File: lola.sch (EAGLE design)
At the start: 1 part, among them U1 ATMEGA328P_TQFP

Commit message: Base modules
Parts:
- added C1, C11, C14, C2, C3, C4, C7, C8, C9: 0.1uF, resistor:C-EUC0603
- added C10, C12, C13: 4.7uF, resistor:C-EUC0603
- added C5, C6: 22pF, resistor:C-EUC0603
- added CN1: (no value), adafruit:USBMINIB
- added D1, D2: transil, SparkFun-DiscreteSemi:DIODE-SCHOTTKY-BAT20J
- added D3: DIODE-SCHOTTKY-B340A, SparkFun-DiscreteSemi:DIODE-SCHOTTKY-B340A
- added F1, F3: 6V/0.5A, SparkFun-Fuses:PPTC_HALF-AMP
- added F2: (no value), adafruit:PTCFUSE-1812
- added IC1: FT232RL, ftdichip:FT232RL
- added IC2: MCP73833-UN, adafruit:MCP73833-UN
- added L1: LQH32PN4R7NN0L, rcl:L-EUL1812
- added LED1, LED2: (no value), adafruit:LEDCHIPLED_0805
- added Q1: MOSFET_PCH-DMG2307L, SparkFun-DiscreteSemi:MOSFET_PCH-DMG2307L
- added R1, R5, R6, R9: 10K, resistor:R-EU_R0603
- added R2: 1M, resistor:R-EU_R0603
- added R3, R4: 1K, resistor:R-EU_R0603
- added R7: 2K, resistor:R-EU_R0603
- added R8: 10K ntc, resistor:R-EU_R0603
- added U$1: MCP1603T-330I/OS, MCP1603T-330I_OS:MCP1603T-330I/OS
- added U$2, U$3: COMF_BHC-18650-1P, FloManEagle:COMF_BHC-18650-1P
- added U2: RFM69HW, SparkFun-RF:RFM69HW
- added U3: AT24C256C-SSHL-T, AT24C256C-SSHL-T:AT24C256C-SSHL-T
- added U4: ADS1115IDGST, ADS1115IDGST:ADS1115IDGST
- added X1: (no value), adafruit:SMACONNECTOR_EDGE_UFL
- added Y1: 8MHz, SparkFun-Clocks:CRYSTAL-GROUNDEDSMD-5X3.2
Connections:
- new net !EXT_RESET: C8.2, IC1.!RTS
- new net !RESET: C8.1, R1.2, U1.PC6(/RESET)
- new net 3.3V: C1.1, C10.1, C11.1, C14.1, C2.1, C3.1, C4.1, C9.1, F3.2, R1.1, R5.2, R6.2, U1.AREF, U1.AVCC, U1.VCC@4, U1.VCC@6, U2.3.3V, U3.VCC, U4.VDD
- new net 5V: D3.A, F1.2, IC1.VCC, IC2.VDD1, IC2.VDD2, Q1.G, R9.2
- new net ADC_RDY: U4.ALERT/RDY
- new net AIN0: U4.AIN0
- new net AIN1: U4.AIN1
- new net AIN2: U4.AIN2
- new net AIN3: U4.AIN3
- new net CHG: IC2.STAT1
- new net FT_3.3V: C7.1, IC1.3V3OUT, IC1.VCCIO, R3.2, R4.2
- new net FULL: IC2.STAT2
- new net GND: C1.2, C10.2, C11.2, C12.2, C13.2, C14.2, C2.2, C3.2, C4.2, C5.2, C6.2, C7.2, C9.2, CN1.GND, D1.A, D2.A, IC1.GND@A, IC2.GND, R7.2, R8.2, R9.1, U$1.GND, U$2.GND, U$3.GND, U1.AGND, U1.GND@3, U1.GND@5, U2.GND@1, U2.GND@2, U3.A0, U3.A1, U3.A2, U3.GND, U3.WP, U4.ADDR, U4.GND, X1.GND1, X1.GND2, X1.GND3, X1.GND4, Y1.3
- new net MISO: U1.PB4(MISO), U2.MISO
- new net MOSI: U1.PB3(MOSI/OC2), U2.MOSI
- new net N$1: U2.ANT, X1.ANT
- new net N$10: U1.PD4(XCK/T0)
- new net N$11: U1.PD5(T1)
- new net N$12: U1.PD6(AIN0)
- new net N$13: U1.PD7(AIN1)
- new net N$14: U1.PB0(ICP)
- new net N$15: U1.PB1(OC1A)
- new net N$16: U1.PB2(SS/OC1B)
- new net N$17: C5.1, R2.2, U1.PB6(XTAL1/TOSC1), Y1.1
- new net N$18: C6.1, R2.1, U1.PB7(XTAL2/TOSC2), Y1.2
- new net N$19: IC2.THERM, R8.1
- new net N$2: F2.1, U$2.BAT
- new net N$20: CN1.VBUS, F1.1
- new net N$21: CN1.D+, D2.C, IC1.USBDP
- new net N$22: CN1.D-, D1.C, IC1.USBDM
- new net N$23: LED2.A, R4.1
- new net N$24: IC1.CBUS1, LED2.C
- new net N$25: IC1.CBUS0, LED1.C
- new net N$26: LED1.A, R3.1
- new net N$28: IC2.PROG, R7.1
- new net N$29: L1.2, U$1.LX
- new net N$3: C13.1, F3.1, L1.1, U$1.VFB/VOUT
- new net N$4: U1.PC0(ADC0)
- new net N$5: U1.PC1(ADC1)
- new net N$6: U1.PC2(ADC2)
- new net N$7: U1.PC3(ADC3)
- new net N$8: U1.PD2(INT0)
- new net N$9: U1.PD3(INT1)
- new net RF_INT: U2.DIO0
- new net RF_SS: U2.NSS
- new net RX: IC1.TXD, U1.PD0(RXD)
- new net SCK: U1.PB5(SCK), U2.SCK
- new net SCL: R5.1, U1.PC5(ADC5/SCL), U3.SCL, U4.SCL
- new net SDA: R6.1, U1.PC4(ADC4/SDA), U3.SDA, U4.SDA
- new net TX: IC1.RXD, U1.PD1(TXD)
- new net VCC: D3.C, Q1.S, U$1.VIN, U$1.~SHDN
- new net V_BATT: C12.1, F2.2, IC2.VBAT1, IC2.VBAT2, Q1.D, U$3.BAT
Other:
- note added: "A0"
- note added: "A1"
- note added: "A2"
- note added: "A3"

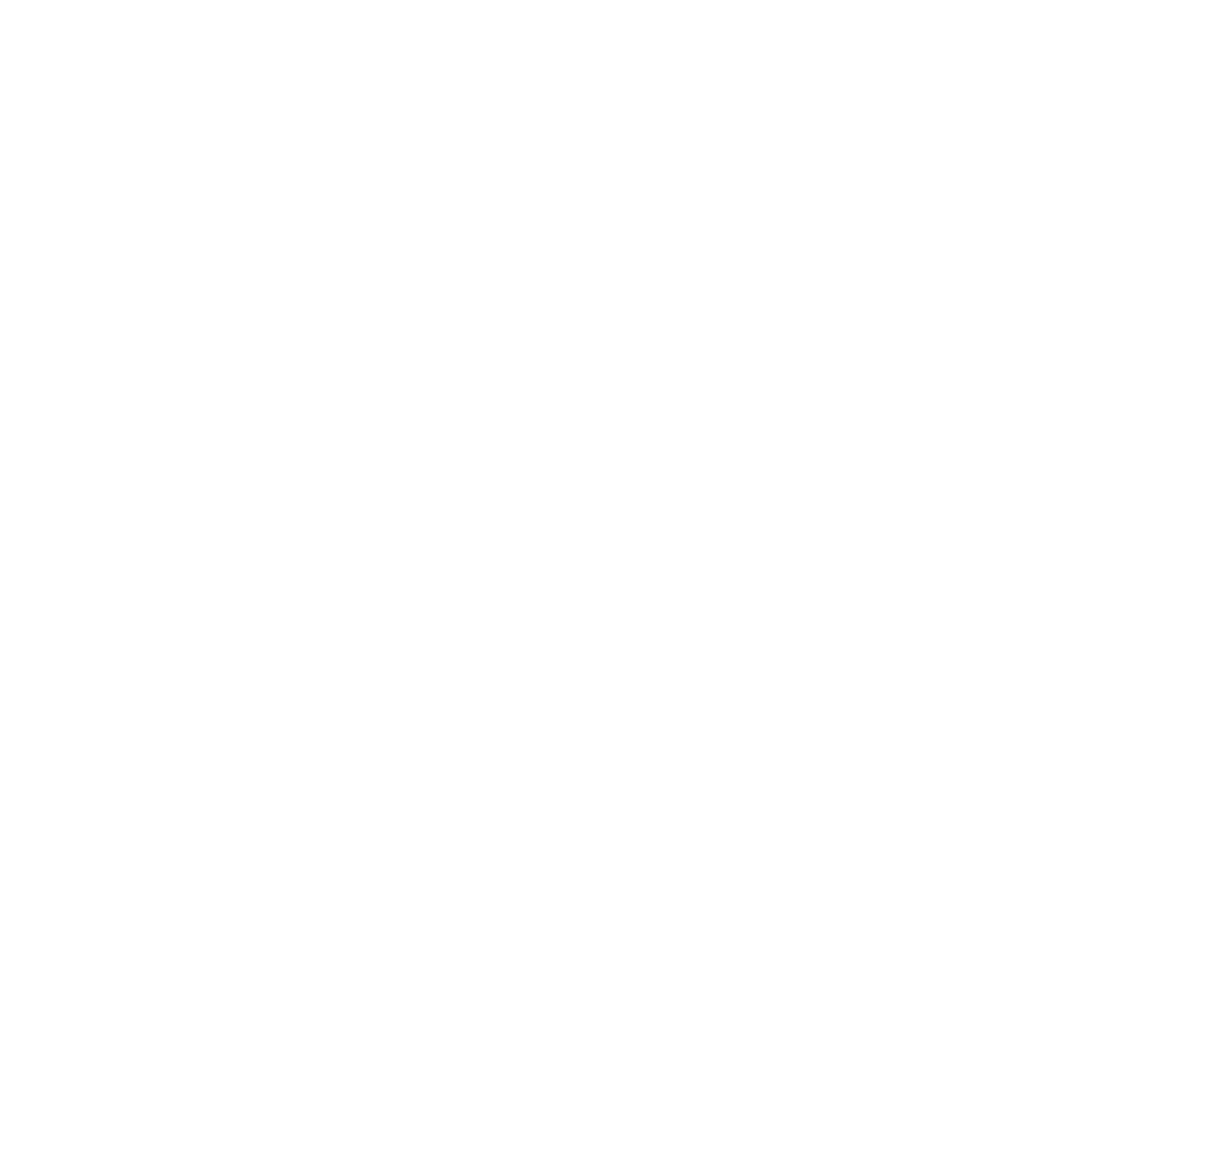
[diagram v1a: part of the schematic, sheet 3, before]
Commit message: StepUp converter plus output-en
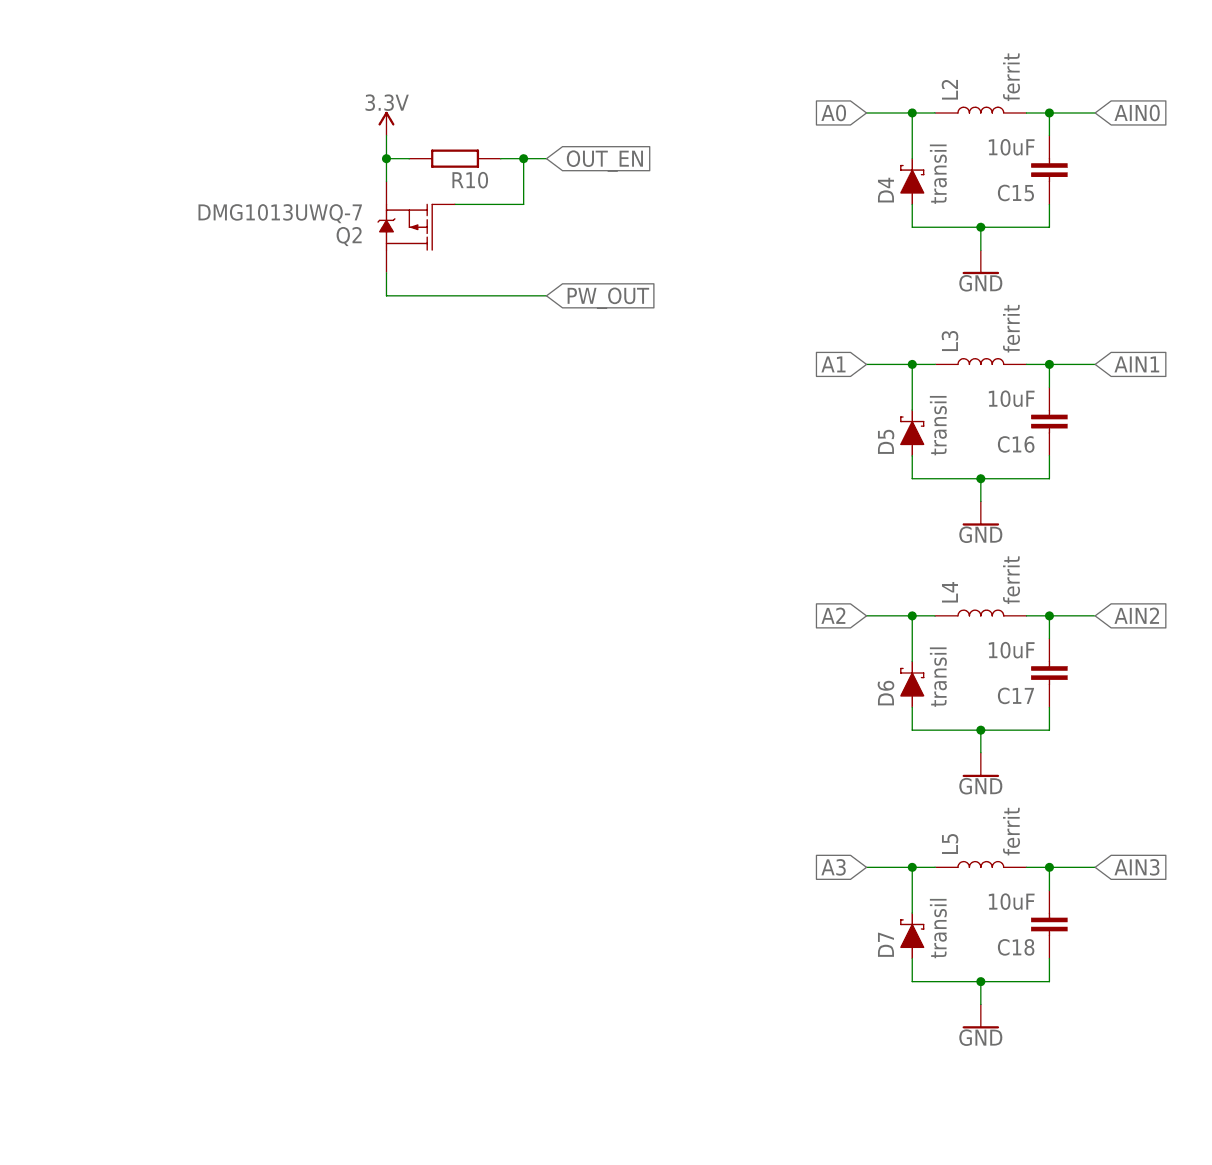
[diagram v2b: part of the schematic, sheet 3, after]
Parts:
- added C15, C16, C17, C18: 10uF, resistor:C-EUC0603
- added C19, C20, C21: 10uF, resistor:C-EUC1206
- added C22: 1uF, resistor:C-EUC0805
- added D4, D5, D6, D7: transil, SparkFun-DiscreteSemi:DIODE-SCHOTTKY-BAT20J
- added L2, L3, L4, L5: ferrit, SparkFun-Coils:INDUCTOR-0603-33NH
- added Q2, Q3: DMG1013UWQ-7, SparkFun-DiscreteSemi:MOSFET_PCH-DMG2307L
- added R10: (no value), resistor:R-EU_R0603
- added R11, R12: 100K, resistor:R-EU_R0603
- added S1: MOMENTARY-SWITCH-SPST-SMD-4.6X2.8MM, SparkFun-Switches:MOMENTARY-SWITCH-SPST-SMD-4.6X2.8MM
- added U$5: MCP1252-33X50I/MS, MCP1252-33X50I_MS:MCP1252-33X50I/MS
- C13: device resistor:C-EUC0603 -> resistor:C-EUC1206
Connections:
- new net 5V_OUT: Q3.D
- new net A0: D4.C, L2.1
- new net A1: D5.C, L3.1
- new net A2: D6.C, L4.1
- new net A3: D7.C, L5.1
- new net BATT_SENSE: R11.1, R12.2
- new net BUCK_EN: U$5.!SHDN
- new net BUCK_PGD: U$5.PGOOD
- new net N$30: C20.1, Q3.S, U$5.VOUT
- new net N$31: C22.1, U$5.C+
- new net N$32: C22.2, U$5.C-
- new net OUT_EN: Q2.G, Q3.G, R10.1
- new net PW_OUT: Q2.D
- net !RESET: now also S1.1
- net 3.3V: now also Q2.S, R10.2
- net AIN0: now also C15.2, L2.2
- net AIN1: now also C16.2, L3.2
- net AIN2: now also C17.2, L4.2
- net AIN3: now also C18.2, L5.2
- net GND: now also C15.1, C16.1, C17.1, C18.1, C19.2, C20.2, C21.1, D4.A, D5.A, D6.A, D7.A, R12.1, S1.2, U$5.GND, U$5.SELECT
- net VCC: now also C21.2
- net V_BATT: now also C19.1, R11.2, U$5.VIN
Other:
- note added: "3.3V DC-DC Converter"
- note added: "5V Buck Converter"
- note added: "Li-ion Charger"
- note added: "X7R Dielectric"
- moved on the sheet: L1

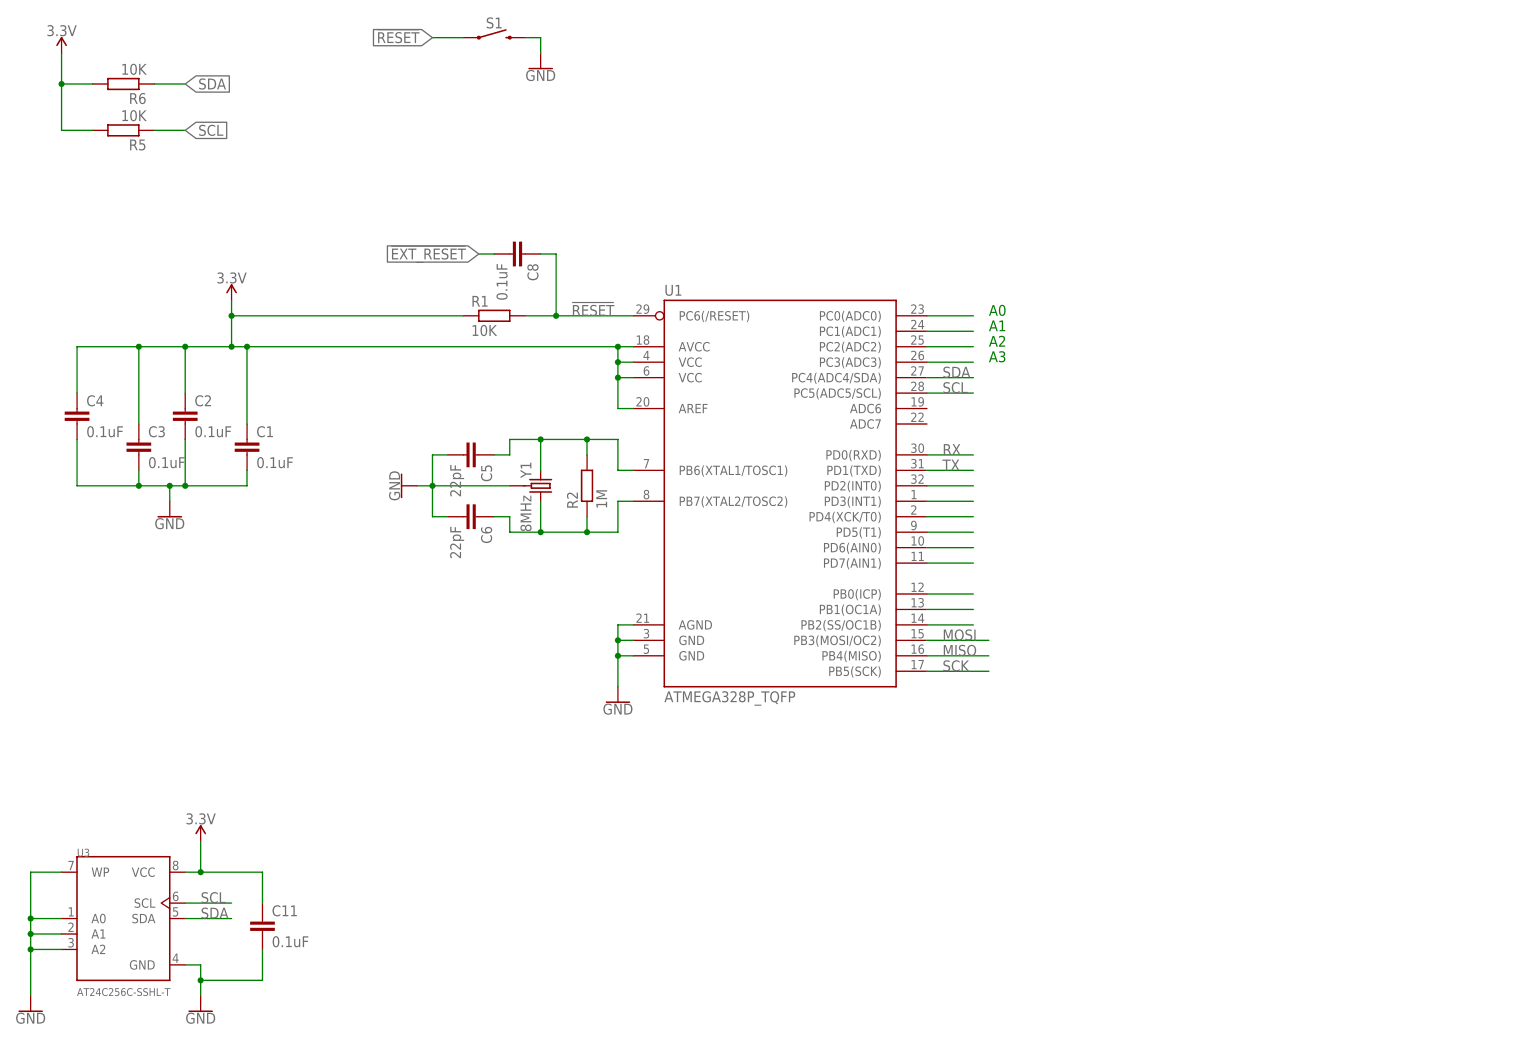
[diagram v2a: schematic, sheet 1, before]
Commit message: rtc, step-up converter
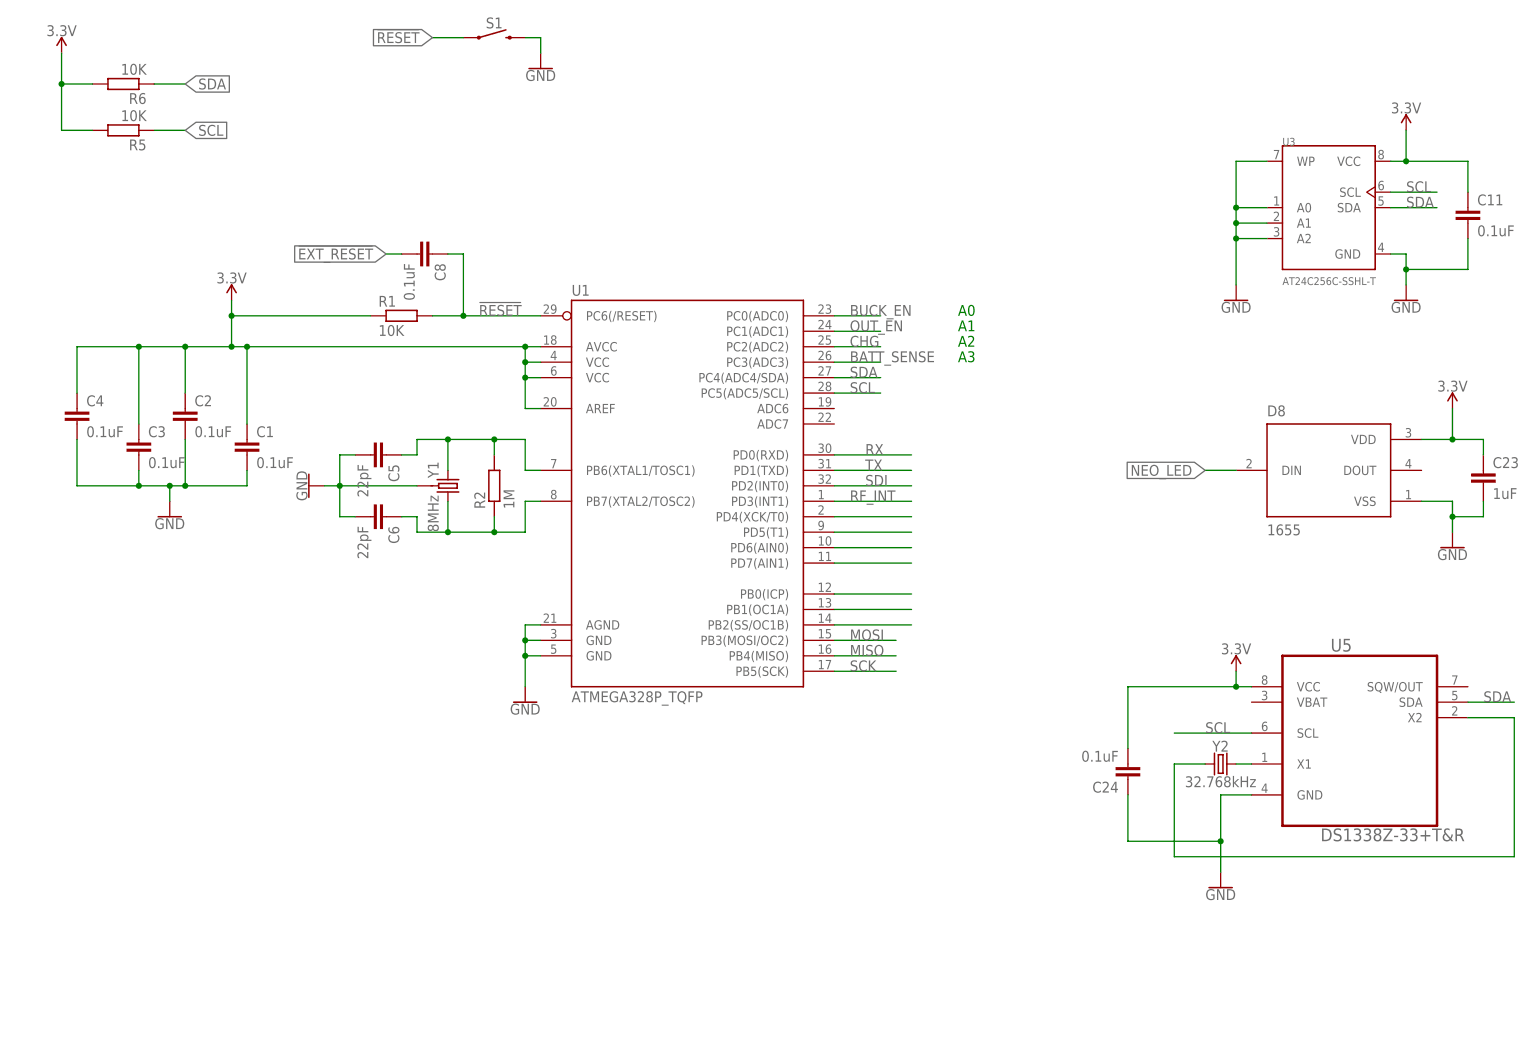
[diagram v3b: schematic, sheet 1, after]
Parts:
- added C23: 1uF, resistor:C-EUC0603
- added C24: 0.1uF, resistor:C-EUC0603
- added D8: 1655, 1655:1655
- added D9: transil, SparkFun-DiscreteSemi:DIODE-SCHOTTKY-BAT20J
- added J4: (no value), SparkFun-Connectors:CONN_025MM
- added J7: (no value), SparkFun-Connectors:CONN_063.5MM-6
- added JP1, JP2, JP3: JUMPER-SMT_2_NO_NO-SILK, SparkFun-Jumpers:JUMPER-SMT_2_NO_NO-SILK
- added LED3, LED4: (no value), adafruit:LEDCHIPLED_0805
- added R13, R14: 2K, resistor:R-EU_R0603
- added U5: DS1338Z-33+T&R, DS1338Z-33_T_R:DS1338Z-33+T&R
- added Y2: 32.768kHz, SparkFun-Clocks:CRYSTAL-32.768KHZSMD-3.2X1.5
- R10: value (none) -> 10K
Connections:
- removed net N$4: U1.PC0(ADC0)
- removed net N$9: U1.PD3(INT1)
- new net NEO_LED: D8.DIN
- new net RMISO: JP1.1, U2.MISO
- new net RMOSI: JP2.1, U2.MOSI
- new net RSCK: JP3.1, U2.SCK
- new net SDI: D9.C, J7.5, U1.PD2(INT0)
- net 3.3V: now also C23.1, C24.2, D8.VDD, U5.VCC
- net 5V_OUT: now also J7.6, R14.1
- net A0: now also J7.4
- net A1: now also J7.3
- net A2: now also J7.2
- net A3: now also J7.1
- net BATT_SENSE: now also U1.PC3(ADC3)
- net BUCK_EN: now also U1.PC0(ADC0)
- net CHG: now also U1.PC2(ADC2)
- net GND: now also C23.2, C24.1, D8.VSS, D9.A, J4.2, LED3.C, LED4.C, U5.GND
- net MISO: now also JP1.2; no longer U2.MISO
- net MOSI: now also JP2.2; no longer U2.MOSI
- net N$5: now also LED3.A, R14.2; no longer U1.PC1(ADC1)
- net N$6: now also U5.X1, Y2.2; no longer U1.PC2(ADC2)
- net N$7: now also U5.X2, Y2.1; no longer U1.PC3(ADC3)
- net N$8: now also LED4.A, R13.2; no longer U1.PD2(INT0)
- net OUT_EN: now also U1.PC1(ADC1)
- net PW_OUT: now also J4.1, R13.1
- net RF_INT: now also U1.PD3(INT1)
- net SCK: now also JP3.2; no longer U2.SCK
- net SCL: now also U5.SCL
- net SDA: now also U5.SDA
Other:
- moved on the sheet: C10, C11, C5, C6, C8, C9, R1, R2, U1, U3, Y1

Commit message: Feliratozás van hátra + kondi + buzzer
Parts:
- added C25, C26: 0.1uF, resistor:C-EUC0603
- added J1: (no value), SparkFun-Connectors:CONN_04LOCK_LONGPADS
- added J3: (no value), SparkFun-Connectors:CONN_06NO_SILK_FEMALE_PTH
- added S2: MOMENTARY-SWITCH-SPST-SMD-4.6X2.8MM, SparkFun-Switches:MOMENTARY-SWITCH-SPST-SMD-4.6X2.8MM
- added U$4: OLED_0.96_I2C, tft_1.8_1.44_oled_0.96:OLED_0.96_I2C
- added U6: SHT21, SHT21:SHT21
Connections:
- removed net N$10: U1.PD4(XCK/T0)
- removed net N$11: U1.PD5(T1)
- removed net N$12: U1.PD6(AIN0)
- removed net N$16: U1.PB2(SS/OC1B)
- new net SW: S2.1, U1.PB2(SS/OC1B)
- net !RESET: now also J3.3
- net 3.3V: now also C25.1, C26.2, J1.2, J3.1, U$4.VCC, U6.VDD
- net ADC_RDY: now also U1.PD5(T1)
- net GND: now also C25.2, C26.1, J1.1, J3.2, S2.2, U$4.GND, U6.VSS
- net MISO: now also J3.5
- net MOSI: now also J3.6
- net NEO_LED: now also U1.PD4(XCK/T0)
- net RF_SS: now also U1.PD6(AIN0)
- net SCK: now also J3.4
- net SCL: now also J1.4, U$4.SCL, U6.SCL
- net SDA: now also J1.3, U$4.SDA, U6.SDA

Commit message: v1
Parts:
- added C27: 100uF, resistor:CPOL-EUCT6032
- added LED5: (no value), adafruit:LEDCHIPLED_0805
- added R15: 10K, resistor:R-EU_R0603
- added T1, T2: (no value), transistor:MUN2211T1-NPN_DRIVER-SC59-BEC
- added U$8: BUZZER_5X9.6, FloManEagle:BUZZER_5X9.6
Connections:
- removed net N$14: U1.PB0(ICP)
- removed net N$15: U1.PB1(OC1A)
- new net BUZZER: T1.B, U1.PB0(ICP)
- new net LED: T2.B, U1.PB1(OC1A)
- new net N$11: T1.C, U$8.GND
- new net N$4: LED5.A, R15.1
- new net N$9: LED5.C, T2.C
- net 3.3V: now also R15.2, U$8.VCC
- net 5V: now also C27.+
- net GND: now also C27.-, T1.E, T2.E
